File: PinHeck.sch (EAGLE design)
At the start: 341 parts, among them IC1 FT232RL-REEL, IC2 PIC32MX795F512L-80I/PT, IC3 CD74HCT244E, IC4 CD74HCT244E, IC5 ULN2803A, J1 500075-1517, J11 No Load, J2 500075-1517, J3 N/A, J6 161-3507-E, P1 TC33X-2-103E, SW1 101-0134-EV, SW2 101-0134-EV, SW3 101-0134-EV, SW4 0S102011MS2QS1, U1 P8X32A-Q44, U10 74HCT2G04GV,125, U11 74HC165D,652, U12 74HC165D,652, U14 MC74HC08ADG, U15 MC74HC08ADG, U16 MC74HC08ADG, U17 MC74HC08ADG, U18 MC74HC08ADG, U19 MC74HC08ADG, U2 FT230XS-R, U20 TIP107, U21 TIP107, U22 TIP107, U23 TIP107, U24 TIP107, U25 TIP107, U26 TIP107, U27 TIP107, U28 TIP102, U29 TIP102, U3 74HC595D-Q100, U30 TIP102, U31 TIP102, U32 TIP102, U33 TIP102, U34 TIP102, U35 TIP102, U36 WS2801, U37 TIP102, U38 WS2801, U39 LM2937IMP-3.3/NOPB, U4 24LC1025-I/P, U40 TIP102, U41 TIP102, U42 TIP102, U43 TIP102, U44 TIP102, U45 TIP102, U46 TIP102, U47 TIP102, U48 TIP102, U49 TIP102, U5 74HC595D-Q100, U50 TIP102, U51 TIP102, U52 CD74HC123M96, U6 TIP102, U7 TIP102, U8 TIP102, U9 TIP102, X1 FQ7050B-8.000, X2 ECS-65-20-4X

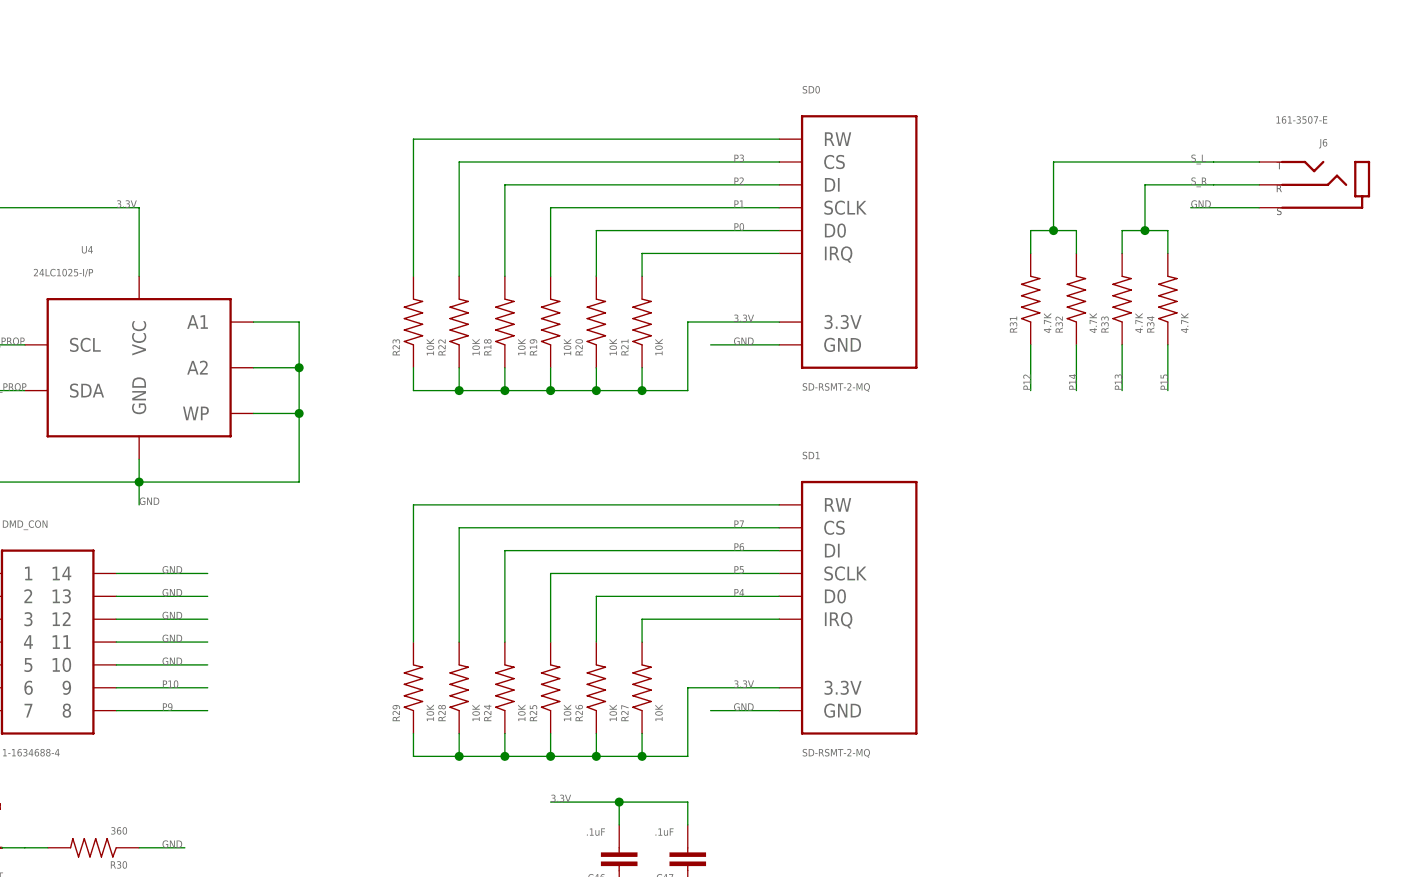
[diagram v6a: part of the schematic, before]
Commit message: Added 2 more audio channels
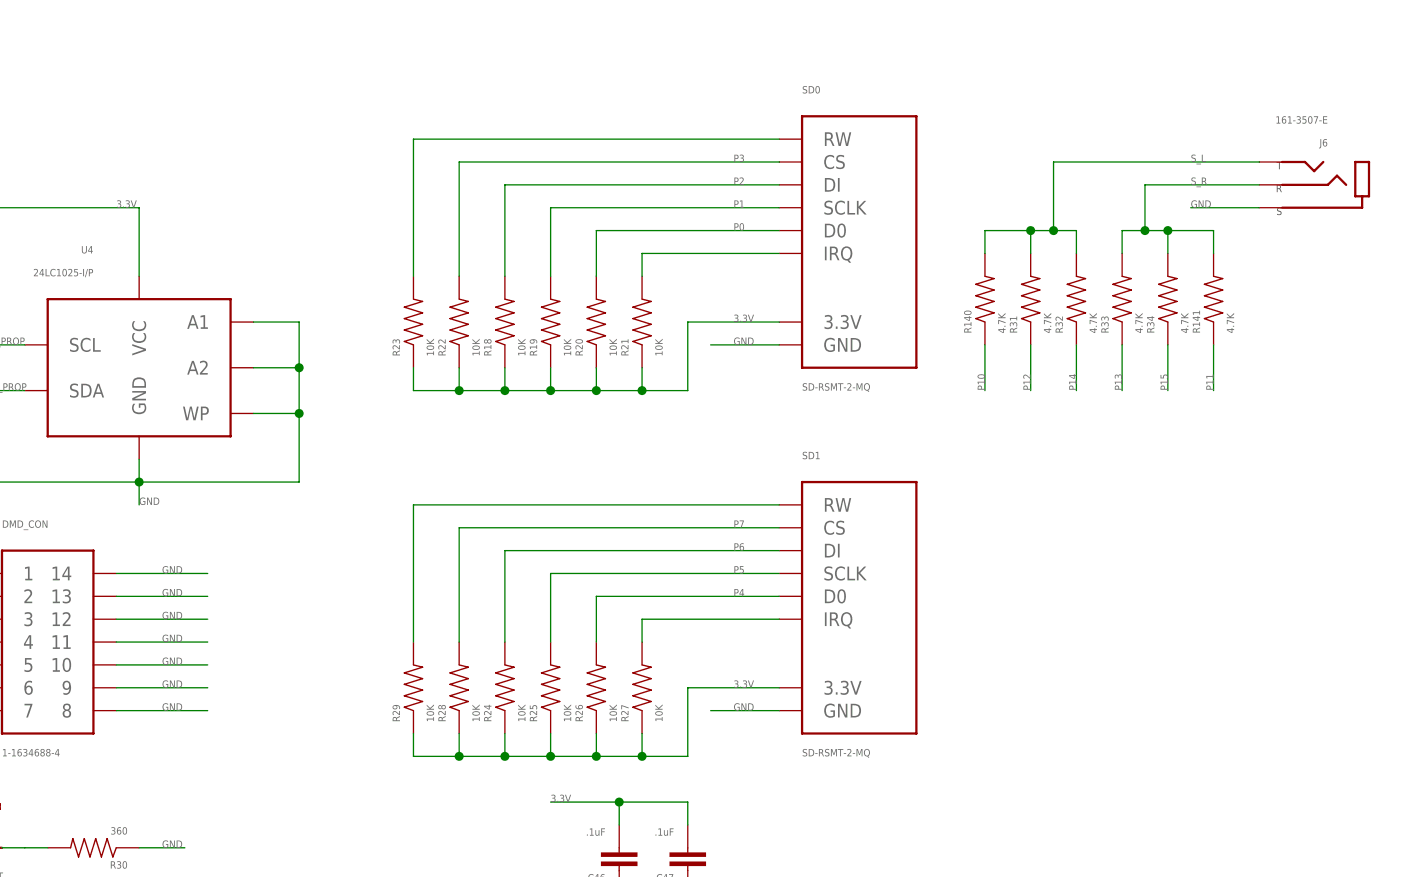
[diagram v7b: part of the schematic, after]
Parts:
- added R140, R141: 4.7K, PP_Passives:RESISTOR0805
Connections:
- net GND: now also DMD_CON.8, DMD_CON.9
- net P10: now also R140.1; no longer DMD_CON.9
- net P11: now also R141.1
- net P9: no longer DMD_CON.8
- net S_L: now also R140.2
- net S_R: now also R141.2
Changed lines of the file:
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@@
 <part name="R138" library="PP_Passives" deviceset="RESISTOR" device="0805" value="10K"/>
 <part name="R139" library="PP_Passives" deviceset="RESISTOR" device="0805" value="10K"/>
+<part name="R140" library="PP_Passives" deviceset="RESISTOR" device="0805" value="4.7K"/>
+<part name="R141" library="PP_Passives" deviceset="RESISTOR" device="0805" value="4.7K"/>
 </parts>
 <sheets>
@@
 <instance part="R138" gate="G$1" x="535.94" y="-58.42" rot="MR270"/>
 <instance part="R139" gate="G$1" x="535.94" y="-78.74" rot="MR270"/>
+<instance part="R140" gate="G$1" x="248.92" y="17.78" rot="R90"/>
+<instance part="R141" gate="G$1" x="274.32" y="17.78" rot="R90"/>
 </instances>
 <busses>
@@
 <label x="541.02" y="-86.36" size="0.8128" layer="95" font="vector"/>
 </segment>
+<segment>
+<pinref part="DMD_CON" gate="G$1" pin="9"/>
+<wire x1="162.56" y1="-25.4" x2="152.4" y2="-25.4" width="0.1524" layer="91"/>
+<label x="157.48" y="-25.4" size="0.8128" layer="95" font="vector"/>
+</segment>
+<segment>
+<pinref part="DMD_CON" gate="G$1" pin="8"/>
+<wire x1="152.4" y1="-27.94" x2="162.56" y2="-27.94" width="0.1524" layer="91"/>
+<label x="157.48" y="-27.94" size="0.8128" layer="95" font="vector"/>
+</segment>
 </net>
 <net name="N$4" class="0">
@@
 <label x="55.88" y="-15.24" size="0.8128" layer="95" font="vector"/>
 </segment>
+<segment>
+<pinref part="R141" gate="G$1" pin="1"/>
+<wire x1="274.32" y1="12.7" x2="274.32" y2="7.62" width="0.1524" layer="91"/>
+<label x="274.32" y="7.62" size="0.8128" layer="95" font="vector" rot="R90"/>
+</segment>
 </net>
 <net name="P10" class="0">
@@
 </segment>
 <segment>
-<pinref part="DMD_CON" gate="G$1" pin="9"/>
-<wire x1="162.56" y1="-25.4" x2="152.4" y2="-25.4" width="0.1524" layer="91"/>
-<label x="157.48" y="-25.4" size="0.8128" layer="95" font="vector"/>
+<pinref part="R140" gate="G$1" pin="1"/>
+<wire x1="248.92" y1="12.7" x2="248.92" y2="7.62" width="0.1524" layer="91"/>
+<label x="248.92" y="7.62" size="0.8128" layer="95" font="vector" rot="R90"/>
 </segment>
 </net>
@@
 <label x="55.88" y="-10.16" size="0.8128" layer="95" font="vector"/>
 </segment>
-<segment>
-<pinref part="DMD_CON" gate="G$1" pin="8"/>
-<wire x1="152.4" y1="-27.94" x2="162.56" y2="-27.94" width="0.1524" layer="91"/>
-<label x="157.48" y="-27.94" size="0.8128" layer="95" font="vector"/>
-</segment>
 </net>
 <net name="P8" class="0">
@@
 <wire x1="259.08" y1="25.4" x2="259.08" y2="22.86" width="0.1524" layer="91"/>
 <wire x1="256.54" y1="25.4" x2="256.54" y2="33.02" width="0.1524" layer="91"/>
-<wire x1="256.54" y1="33.02" x2="274.32" y2="33.02" width="0.1524" layer="91"/>
+<wire x1="256.54" y1="33.02" x2="279.4" y2="33.02" width="0.1524" layer="91"/>
 <junction x="256.54" y="25.4"/>
 <pinref part="J6" gate="G$1" pin="T"/>
-<wire x1="274.32" y1="33.02" x2="279.4" y2="33.02" width="0.1524" layer="91"/>
+<pinref part="R140" gate="G$1" pin="2"/>
+<wire x1="248.92" y1="22.86" x2="248.92" y2="25.4" width="0.1524" layer="91"/>
+<wire x1="248.92" y1="25.4" x2="254" y2="25.4" width="0.1524" layer="91"/>
+<junction x="254" y="25.4"/>
 </segment>
 </net>
 <net name="S_R" class="0">
 <segment>
-<wire x1="274.32" y1="30.48" x2="266.7" y2="30.48" width="0.1524" layer="91"/>
+<wire x1="279.4" y1="30.48" x2="266.7" y2="30.48" width="0.1524" layer="91"/>
 <label x="271.78" y="30.48" size="0.8128" layer="95" font="vector"/>
 <pinref part="R33" gate="G$1" pin="2"/>
@@
 <junction x="266.7" y="25.4"/>
 <pinref part="J6" gate="G$1" pin="R"/>
-<wire x1="279.4" y1="30.48" x2="274.32" y2="30.48" width="0.1524" layer="91"/>
+<pinref part="R141" gate="G$1" pin="2"/>
+<wire x1="274.32" y1="22.86" x2="274.32" y2="25.4" width="0.1524" layer="91"/>
+<wire x1="274.32" y1="25.4" x2="269.24" y2="25.4" width="0.1524" layer="91"/>
+<junction x="269.24" y="25.4"/>
 </segment>
 </net>

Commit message: Added MF Logo
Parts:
- added U$2: MF_LOGOLOGO_TEXT, PP_Aesthetics:MF_LOGOLOGO_TEXT
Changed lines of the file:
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@@
 <part name="R140" library="PP_Passives" deviceset="RESISTOR" device="0805" value="4.7K"/>
 <part name="R141" library="PP_Passives" deviceset="RESISTOR" device="0805" value="4.7K"/>
+<part name="U$2" library="PP_Aesthetics" deviceset="MF_LOGO" device="LOGO_TEXT"/>
 </parts>
 <sheets>
@@
 <instance part="R140" gate="G$1" x="248.92" y="17.78" rot="R90"/>
 <instance part="R141" gate="G$1" x="274.32" y="17.78" rot="R90"/>
+<instance part="U$2" gate="G$1" x="307.34" y="-63.5"/>
 </instances>
 <busses>
